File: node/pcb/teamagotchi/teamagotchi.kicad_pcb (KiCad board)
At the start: 2 copper layers, 2 parts

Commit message: first shot of the pcv
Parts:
- removed A1: Adafruit_Feather_Generic, Module:Adafruit_Feather
- removed BT1: Battery, Battery:BatteryHolder_Keystone_103_1x20mm
- added R1: R, Resistor_THT:R_Axial_DIN0204_L3.6mm_D1.6mm_P7.62mm_Horizontal, F.Cu at (173.5, 108.3)
- added R2: R, Resistor_THT:R_Axial_DIN0204_L3.6mm_D1.6mm_P7.62mm_Horizontal, F.Cu at (170.3, 108.3)
- added R3: R, Resistor_THT:R_Axial_DIN0204_L3.6mm_D1.6mm_P7.62mm_Horizontal, F.Cu at (167.2, 108.3)
- added R4: R, Resistor_THT:R_Axial_DIN0204_L3.6mm_D1.6mm_P7.62mm_Horizontal, F.Cu at (164.0, 108.3)
- added R5: R, Resistor_THT:R_Axial_DIN0204_L3.6mm_D1.6mm_P7.62mm_Horizontal, F.Cu at (160.9, 108.3)
- added REF**: MountingHole_2.2mm_M2, MountingHole:MountingHole_2.2mm_M2, F.Cu at (182.5, 49.2)
- added REF**: MountingHole_2.2mm_M2, MountingHole:MountingHole_2.2mm_M2, F.Cu at (112.5, 49.2)
- added REF**: MountingHole_2.2mm_M2, MountingHole:MountingHole_2.2mm_M2, F.Cu at (182.5, 155.6)
- added REF**: MountingHole_2.2mm_M2, MountingHole:MountingHole_2.2mm_M2, F.Cu at (112.5, 155.6)
- added SW1: SW_Push, Button_Switch_THT:SW_SPST_Omron_B3F-40xx, F.Cu at (167.4, 129.3)
- added SW2: SW_Push, Button_Switch_THT:SW_SPST_Omron_B3F-40xx, F.Cu at (130.4, 112.3)
- added SW3: SW_Push, Button_Switch_THT:SW_SPST_Omron_B3F-40xx, F.Cu at (145.9, 129.3)
- added SW4: SW_Push, Button_Switch_THT:SW_SPST_Omron_B3F-40xx, F.Cu at (114.9, 129.3)
- added SW5: SW_Push, Button_Switch_THT:SW_SPST_Omron_B3F-40xx, F.Cu at (130.4, 146.3)
- added TFT1: ~, Library:Display-2.8, F.Cu at (126.7, 92.8)
- added U1: 3406, Library:MODULE_3406, B.Cu at (156.2, 74.2)
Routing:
- net Net-(TFT1-3/5V): track 0.00 -> 185.0 mm, vias 0 -> 1
- net Net-(U1-A2/0.04): track 0.00 -> 100.9 mm
- net Net-(U1-A4/0.28): track 0.00 -> 78.4 mm
- net Net-(TFT1-GND): track 0.00 -> 75.3 mm, vias 0 -> 1
- net Net-(A1-GND): track 66.5 -> 0.00 mm
- net Net-(U1-A1/0.03): track 0.00 -> 63.3 mm
- net Net-(U1-A3/0.05): track 0.00 -> 56.6 mm
- net Net-(TFT1-D10/TFT_CS): track 0.00 -> 36.8 mm, vias 0 -> 1
- net Net-(TFT1-D9/TFT_DC): track 0.00 -> 36.4 mm
- net Net-(TFT1-D8/Touch_CS): track 0.00 -> 36.3 mm
- net Net-(A1-VBAT): track 27.8 -> 0.00 mm
- net Net-(TFT1-D13/SCLK): track 0.00 -> 25.5 mm
- net Net-(R5-Pad2): track 0.00 -> 18.5 mm
- net Net-(TFT1-D12/MISO): track 0.00 -> 15.0 mm
- net Net-(TFT1-D11/MOSI): track 0.00 -> 15.0 mm
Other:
- board outline added: 75.1 x 111.4 mm

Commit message: first 1.0 of PCB
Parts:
- removed REF** (x4): MountingHole_2.2mm_M2, MountingHole:MountingHole_2.2mm_M2
- added C1: C, Capacitor_THT:C_Disc_D3.0mm_W1.6mm_P2.50mm, B.Cu at (113.9, 79.9)
- added D1: 1N4001, Diode_THT:D_DO-41_SOD81_P10.16mm_Horizontal, B.Cu at (112.6, 67.6)
- added M1: Motor_DC, Connector_Molex:Molex_MicroClasp_55932-0210_1x02_P2.00mm_Vertical, B.Cu at (121.4, 85.1)
- added Q1: BC547, Package_TO_SOT_THT:TO-92_Inline, B.Cu at (125.6, 72.6)
- added R6: R, Resistor_THT:R_Axial_DIN0204_L3.6mm_D1.6mm_P7.62mm_Horizontal, B.Cu at (128.4, 60.6)
- moved TFT1 65.7 mm to (177.9, 51.6)
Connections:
- R5 pad 2: Net-(R5-Pad2) -> Net-(U1-A5/0.29)
- SW2 pad 1: Net-(R5-Pad2) -> Net-(U1-A5/0.29)
- U1 pad 10: unconnected-(U1-A5/0.29-Pad10) -> Net-(U1-A5/0.29)
- U1 pad 22: Net-(TFT1-D9/TFT_DC) -> Net-(TFT1-D10/TFT_CS)
- U1 pad 23: Net-(TFT1-D10/TFT_CS) -> Net-(TFT1-D9/TFT_DC)
- U1 pad 25: unconnected-(U1-P0.16-Pad25) -> Net-(U1-P0.16)
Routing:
- net Net-(U1-P0.16): track 0.00 -> 53.6 mm
- net Net-(U1-A5/0.29): track 0.00 -> 48.5 mm
- net Net-(D1-K): track 185.0 -> 214.8 mm
- net Net-(D1-A): track 0.00 -> 29.5 mm
- net Net-(TFT1-D10/TFT_CS): track 36.8 -> 12.4 mm, vias 1 -> 0
- net Net-(TFT1-D9/TFT_DC): track 36.4 -> 12.4 mm
- net Net-(TFT1-D8/Touch_CS): track 36.3 -> 12.4 mm
- net Net-(Q1-E): track 75.3 -> 96.0 mm
- net Net-(TFT1-D12/MISO): track 15.0 -> 33.9 mm
- net Net-(TFT1-D11/MOSI): track 15.0 -> 33.8 mm
- net Net-(R5-Pad2): track 18.5 -> 0.00 mm
- net Net-(TFT1-D13/SCLK): track 25.5 -> 37.0 mm, vias 0 -> 1
- net Net-(U1-A1/0.03): track 63.3 -> 71.9 mm, vias 0 -> 1
- net Net-(Q1-B): track 0.00 -> 5.00 mm
- net Net-(U1-A2/0.04): track 100.9 -> 104.5 mm
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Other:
- board size 75.1 x 111.4 mm -> 75 x 112 mm
- board text added: "R4"

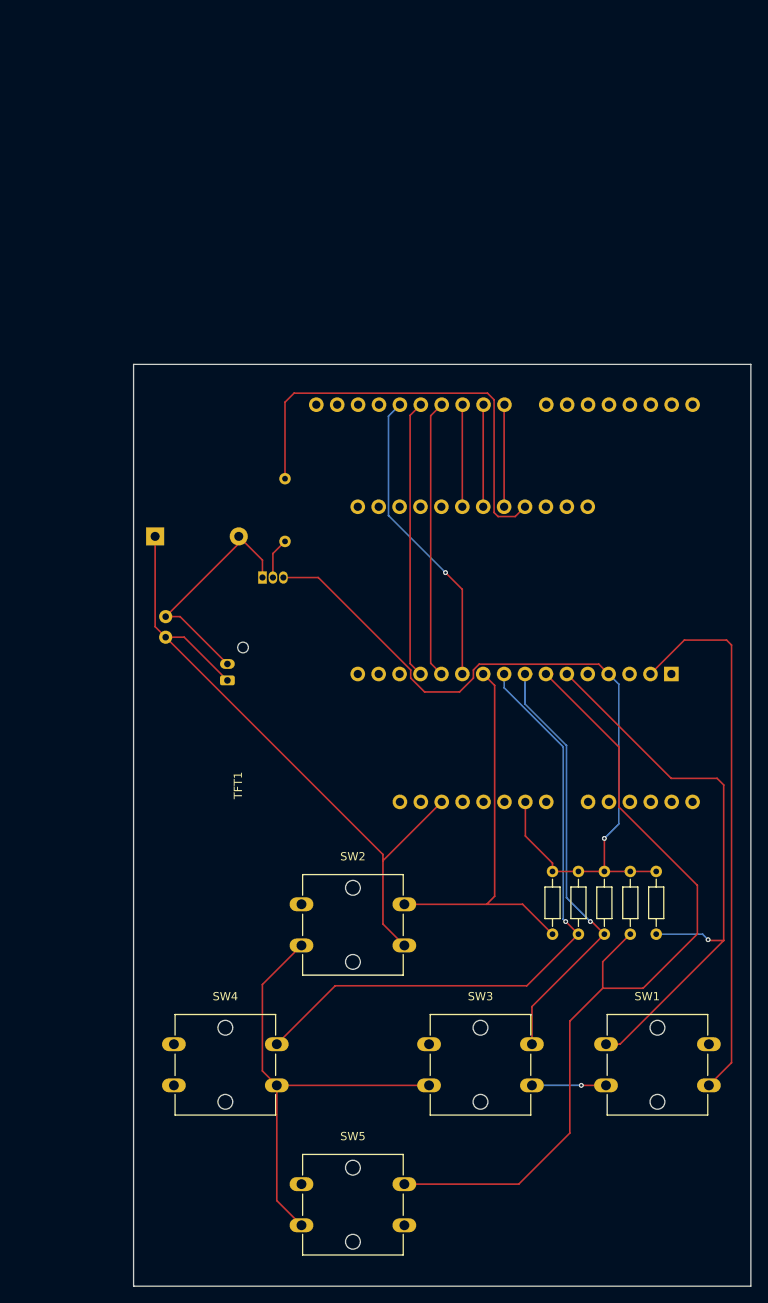
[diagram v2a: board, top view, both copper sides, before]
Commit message: added 3D export
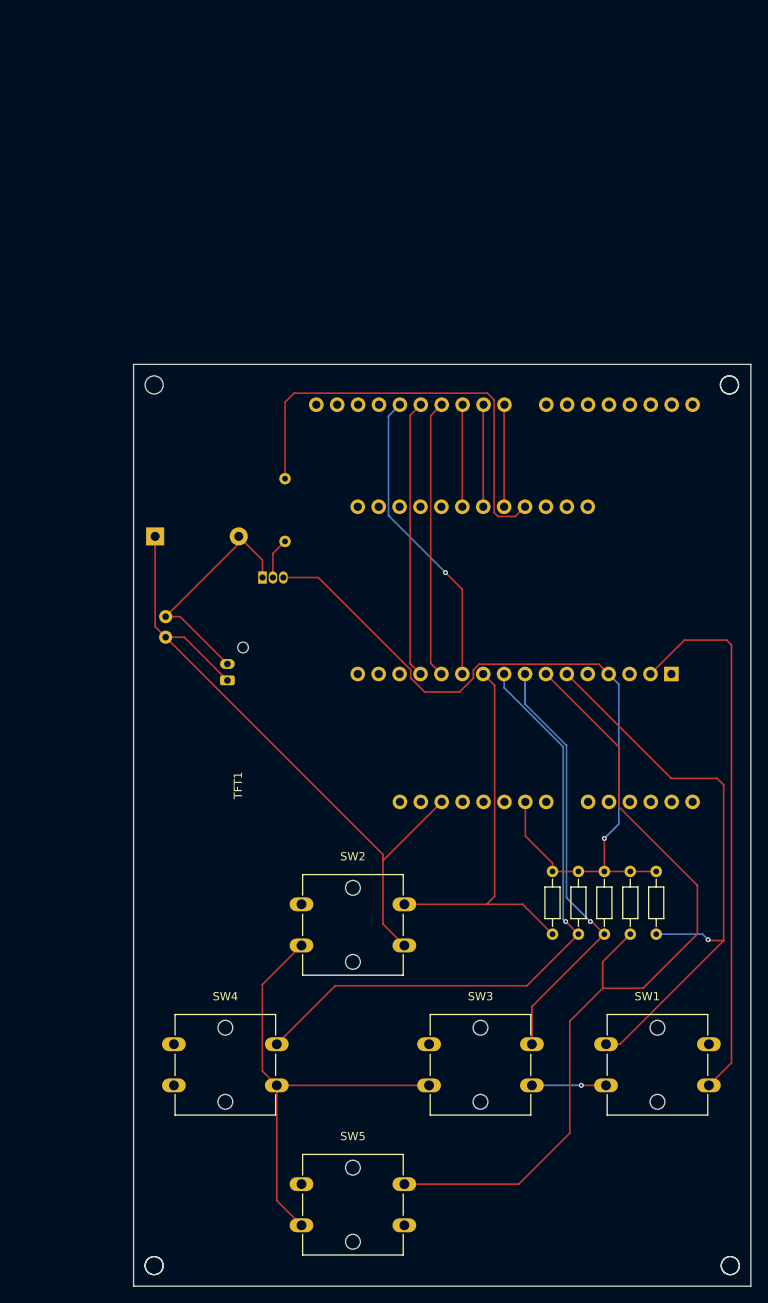
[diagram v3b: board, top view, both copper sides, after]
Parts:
- added ?: , , F.Cu at (182.4, 49.2)
- added ?: , , F.Cu at (112.5, 156.2)
- added ?: , , F.Cu at (182.5, 156.2)
- added REF**: 2.2mm_M2, MountingHole:MountingHole_2.2mm_M2, F.Cu at (112.5, 156.2)
- added REF**: 2.2mm_M2, MountingHole:MountingHole_2.2mm_M2, F.Cu at (182.5, 156.2)
- added REF**: 2.2mm_M2, MountingHole:MountingHole_2.2mm_M2, F.Cu at (112.5, 49.2)
- added REF**: 2.2mm_M2, MountingHole:MountingHole_2.2mm_M2, F.Cu at (182.4, 49.2)

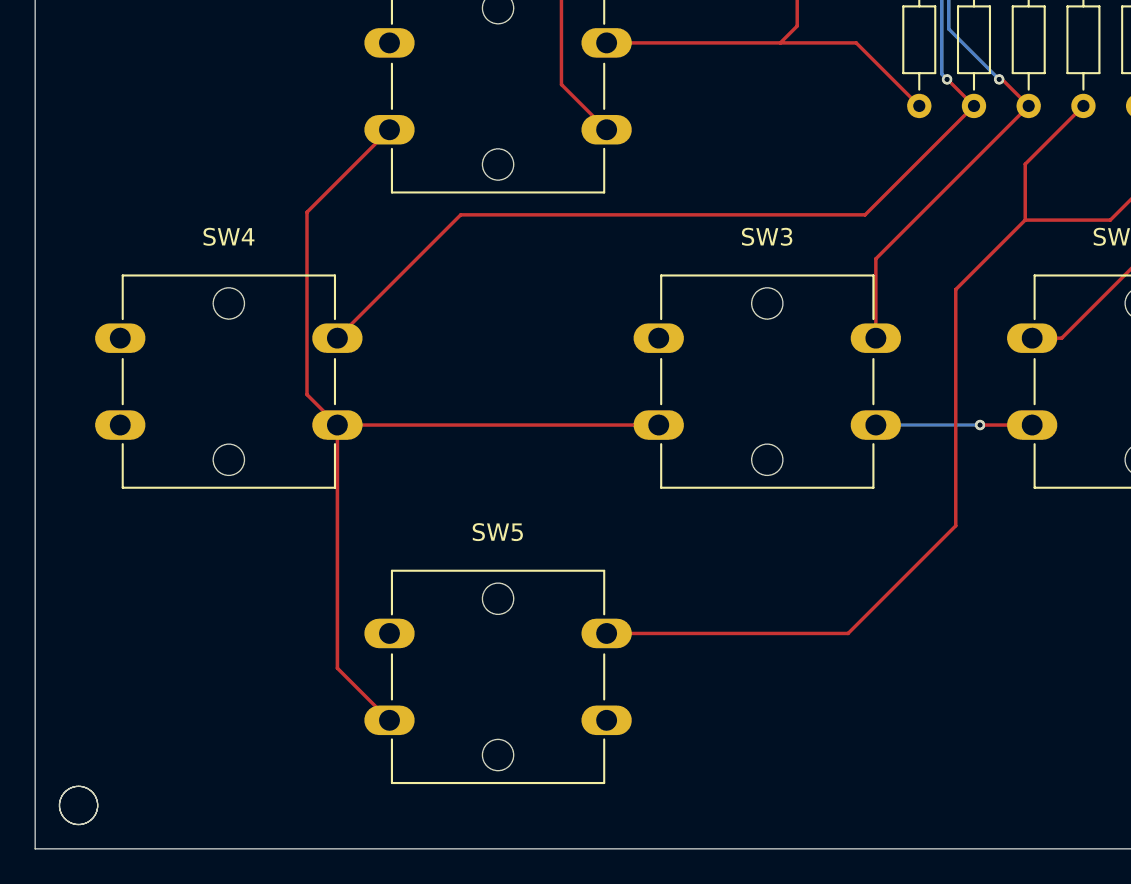
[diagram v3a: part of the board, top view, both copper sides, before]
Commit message: changed the button placement a little bit
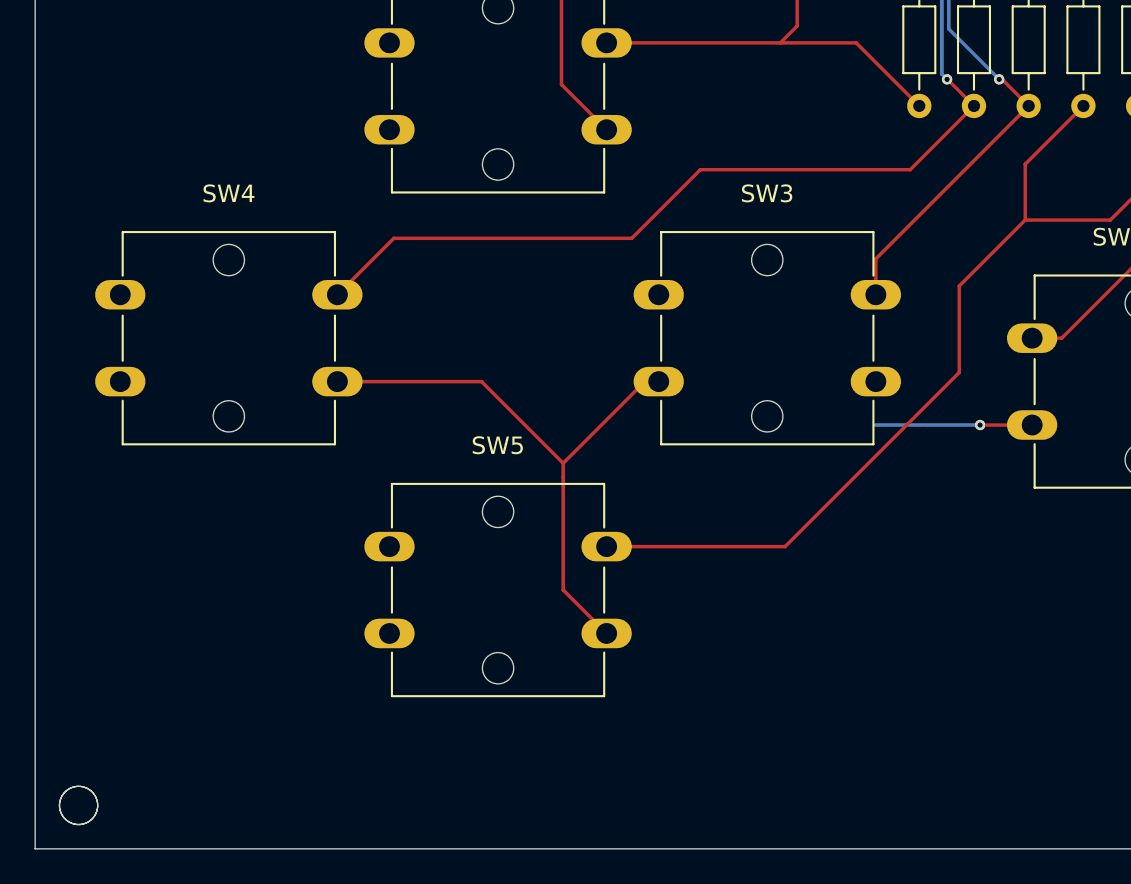
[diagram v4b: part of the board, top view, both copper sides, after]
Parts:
- moved SW5 5.00 mm to (130.4, 141.3)
- moved SW3 2.50 mm to (145.9, 126.8)
- moved SW4 2.50 mm to (114.9, 126.8)
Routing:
- net Net-(D1-K): track 214.8 -> 191.3 mm
- net Net-(U1-A2/0.04): track 104.5 -> 97.1 mm
- net Net-(U1-A3/0.05): track 53.6 -> 51.1 mm
- net Net-(U1-A4/0.28): track 77.6 -> 76.5 mm
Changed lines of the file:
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@@
 	(footprint "Button_Switch_THT:SW_SPST_Omron_B3F-40xx"
 		(layer "F.Cu")
-		(at 130.36 146.306)
+		(at 130.36 141.306)
 		(descr "SW_THT_Tactile_Omron_B3F-40xx, 12x12 mm, Through hole switch from the B3F Family manufactured by Omron,  https://www.omron.com/ecb/products/pdf/en-b3f.pdf")
 		(tags "tactile switch THT button push B3F-4000 B3F-4050 B3F-4005 B3F-4055  ")
@@
 	(footprint "Button_Switch_THT:SW_SPST_Omron_B3F-40xx"
 		(layer "F.Cu")
-		(at 145.86 129.306)
+		(at 145.86 126.806)
 		(descr "SW_THT_Tactile_Omron_B3F-40xx, 12x12 mm, Through hole switch from the B3F Family manufactured by Omron,  https://www.omron.com/ecb/products/pdf/en-b3f.pdf")
 		(tags "tactile switch THT button push B3F-4000 B3F-4050 B3F-4005 B3F-4055  ")
@@
 	(footprint "Button_Switch_THT:SW_SPST_Omron_B3F-40xx"
 		(layer "F.Cu")
-		(at 114.86 129.306)
+		(at 114.86 126.806)
 		(descr "SW_THT_Tactile_Omron_B3F-40xx, 12x12 mm, Through hole switch from the B3F Family manufactured by Omron,  https://www.omron.com/ecb/products/pdf/en-b3f.pdf")
 		(tags "tactile switch THT button push B3F-4000 B3F-4050 B3F-4005 B3F-4055  ")
@@
 	)
 	(segment
-		(start 158.36 129.306)
-		(end 158.36 124.736)
+		(start 158.36 124.736)
+		(end 167.16 115.936)
 		(width 0.2)
 		(layer "F.Cu")
@@
 	)
 	(segment
-		(start 165.63 114.406)
-		(end 167.16 115.936)
+		(start 158.36 126.806)
+		(end 158.36 124.736)
 		(width 0.2)
 		(layer "F.Cu")
@@
 	)
 	(segment
-		(start 158.36 124.736)
+		(start 165.63 114.406)
 		(end 167.16 115.936)
 		(width 0.2)
@@
 	)
 	(segment
-		(start 166.96 122.506)
-		(end 166.96 119.286)
+		(start 142.86 141.306)
+		(end 153.133654 141.306)
 		(width 0.2)
 		(layer "F.Cu")
@@
 	)
 	(segment
-		(start 160.06 84.326)
-		(end 160.9185 84.326)
+		(start 163.16 131.279654)
+		(end 163.16 126.306)
 		(width 0.2)
 		(layer "F.Cu")
@@
 	)
 	(segment
-		(start 168.929 100.475)
-		(end 168.929 93.195)
+		(start 166.96 122.506)
+		(end 166.96 119.286)
 		(width 0.2)
 		(layer "F.Cu")
@@
 	)
 	(segment
-		(start 171.86 122.506)
-		(end 178.46 115.906)
+		(start 160.06 84.326)
+		(end 160.9185 84.326)
 		(width 0.2)
 		(layer "F.Cu")
@@
 	)
 	(segment
-		(start 162.96 140.106)
-		(end 162.96 126.506)
+		(start 168.929 100.475)
+		(end 168.929 93.195)
 		(width 0.2)
 		(layer "F.Cu")
@@
 	)
 	(segment
-		(start 142.86 146.306)
-		(end 156.76 146.306)
+		(start 171.86 122.506)
+		(end 178.46 115.906)
 		(width 0.2)
 		(layer "F.Cu")
@@
 	)
 	(segment
-		(start 162.96 126.506)
-		(end 166.96 122.506)
-		(width 0.2)
-		(layer "F.Cu")
-		(net 23)
-	)
-	(segment
 		(start 178.46 115.906)
 		(end 178.46 110.006)
@@
 	)
 	(segment
-		(start 156.76 146.306)
-		(end 162.96 140.106)
+		(start 163.16 126.306)
+		(end 166.96 122.506)
 		(width 0.2)
 		(layer "F.Cu")
@@
 	)
 	(segment
-		(start 142.86 146.306)
-		(end 143.11 146.056)
+		(start 153.133654 141.306)
+		(end 163.16 131.279654)
 		(width 0.2)
 		(layer "F.Cu")
@@
 	)
 	(segment
-		(start 157.74 122.206)
+		(start 160.34 119.606)
 		(end 164.01 115.936)
 		(width 0.2)
@@
 	)
 	(segment
-		(start 134.46 122.206)
-		(end 157.74 122.206)
+		(start 144.31 123.556)
+		(end 148.26 119.606)
 		(width 0.2)
 		(layer "F.Cu")
@@
 	)
 	(segment
-		(start 164.01 115.936)
-		(end 162.48 114.406)
+		(start 130.61 123.556)
+		(end 144.31 123.556)
+		(width 0.2)
+		(layer "F.Cu")
+		(net 24)
+	)
+	(segment
+		(start 127.36 126.806)
+		(end 130.61 123.556)
+		(width 0.2)
+		(layer "F.Cu")
+		(net 24)
+	)
+	(segment
+		(start 148.26 119.606)
+		(end 160.34 119.606)
 		(width 0.2)
 		(layer "F.Cu")
@@
 	)
 	(segment
-		(start 127.36 129.306)
-		(end 134.46 122.206)
+		(start 164.01 115.936)
+		(end 162.48 114.406)
 		(width 0.2)
 		(layer "F.Cu")
@@
 	)
 	(segment
-		(start 125.61 122.056)
-		(end 125.61 132.556)
+		(start 145.06 131.806)
+		(end 145.86 131.806)
+		(width 0.2)
+		(layer "F.Cu")
+		(net 27)
+	)
+	(segment
+		(start 127.36 131.806)
+		(end 135.66 131.806)
+		(width 0.2)
+		(layer "F.Cu")
+		(net 27)
+	)
+	(segment
+		(start 140.36 136.506)
+		(end 140.36 137.306)
 		(width 0.2)
 		(layer "F.Cu")
@@
 	)
 	(segment
-		(start 125.61 132.556)
-		(end 127.36 134.306)
+		(start 135.66 131.806)
+		(end 140.36 136.506)
 		(width 0.2)
 		(layer "F.Cu")
@@
 	)
 	(segment
+		(start 140.36 136.506)
+		(end 145.06 131.806)
+		(width 0.2)
+		(layer "F.Cu")
+		(net 27)
+	)
+	(segment
 		(start 113.86 79.856)
 		(end 112.58 78.576)
@@
 	)
 	(segment
-		(start 127.36 134.306)
-		(end 127.96 134.306)
+		(start 140.36 143.806)
+		(end 140.36 137.306)
 		(width 0.2)
 		(layer "F.Cu")
@@
 	)
 	(segment
-		(start 130.36 117.306)
-		(end 125.61 122.056)
-		(width 0.2)
-		(layer "F.Cu")
-		(net 27)
-	)
-	(segment
 		(start 116.11 79.856)
 		(end 121.36 85.106)
@@
 	)
 	(segment
-		(start 127.36 148.306)
-		(end 127.36 134.306)
+		(start 142.86 146.306)
+		(end 140.36 143.806)
 		(width 0.2)
 		(layer "F.Cu")
@@
 	)
 	(segment
-		(start 145.86 134.306)
-		(end 127.36 134.306)
-		(width 0.2)
-		(layer "F.Cu")
-		(net 27)
-	)
-	(segment
 		(start 182.61 131.556)
 		(end 179.86 134.306)
@@
 	)
 	(segment
-		(start 130.36 151.306)
-		(end 127.36 148.306)
+		(start 142.86 146.306)
+		(end 143.11 146.056)
 		(width 0.2)
 		(layer "F.Cu")

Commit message: some changes and renders
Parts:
- moved Q1 4.59 mm to (122.1, 75.5)
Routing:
- net Net-(Q1-B): track 5.00 -> 9.40 mm
- net Net-(D1-A): track 29.5 -> 31.5 mm
- net Net-(Q1-E): track 96.0 -> 97.8 mm
- net Net-(D1-K): track 191.3 -> 192.3 mm
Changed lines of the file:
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@@
 			(outputformat 1)
 			(mirror no)
-			(drillshape 1)
+			(drillshape 0)
 			(scaleselection 1)
-			(outputdirectory "")
+			(outputdirectory "gbr/")
 		)
 	)
@@
 			)
 		)
-		(sheetname "Stammblatt")
-		(sheetfile "teamagotchi.kicad_sch")
 		(attr through_hole)
 		(fp_rect
@@
 			(size 1.778 1.778)
 			(drill 1)
-			(layers "*.Cu" "*.Mask" "B.SilkS")
+			(layers "*.Cu" "*.Mask")
 			(remove_unused_layers no)
 		)
@@
 	(footprint "Package_TO_SOT_THT:TO-92_Inline"
 		(layer "B.Cu")
-		(at 125.62 72.606)
+		(at 122.09 75.546)
 		(descr "TO-92 leads in-line, narrow, oval pads, drill 0.75mm (see NXP sot054_po.pdf)")
 		(tags "to-92 sc-43 sc-43a sot54 PA33 transistor")
@@
 	)
 	(segment
-		(start 115.61 77.356)
-		(end 121.36 83.106)
+		(start 122.09 68.256)
+		(end 122.74 67.606)
 		(width 0.2)
 		(layer "F.Cu")
@@
 	)
 	(segment
-		(start 125.62 70.486)
-		(end 122.74 67.606)
+		(start 115.61 77.356)
+		(end 121.36 83.106)
 		(width 0.2)
 		(layer "F.Cu")
@@
 	(segment
 		(start 113.86 77.356)
-		(end 122.74 68.476)
+		(end 113.86 76.486)
 		(width 0.2)
 		(layer "F.Cu")
@@
 	)
 	(segment
-		(start 125.62 72.606)
-		(end 125.62 70.486)
+		(start 113.86 76.486)
+		(end 122.74 67.606)
 		(width 0.2)
 		(layer "F.Cu")
@@
 	)
 	(segment
-		(start 122.74 68.476)
-		(end 122.74 67.606)
+		(start 122.09 75.546)
+		(end 122.09 68.256)
 		(width 0.2)
 		(layer "F.Cu")
@@
 	(segment
 		(start 164.36 134.306)
-		(end 158.36 134.306)
+		(end 161.86 131.806)
 		(width 0.2)
 		(layer "B.Cu")
@@
 	)
 	(segment
-		(start 126.89 69.686)
-		(end 128.36 68.216)
+		(start 161.86 131.806)
+		(end 158.36 131.806)
 		(width 0.2)
-		(layer "F.Cu")
-		(net 28)
+		(layer "B.Cu")
+		(net 27)
 	)
 	(segment
-		(start 126.89 72.606)
-		(end 126.89 69.686)
+		(start 123.36 75.546)
+		(end 123.36 73.216)
 		(width 0.2)
 		(layer "F.Cu")
@@
 	)
 	(segment
-		(start 132.4035 72.606)
-		(end 143.631 83.8335)
+		(start 123.36 73.216)
+		(end 128.36 68.216)
 		(width 0.2)
 		(layer "F.Cu")
-		(net 29)
+		(net 28)
 	)
 	(segment
-		(start 145.3185 86.506)
-		(end 149.5635 86.506)
+		(start 124.63 75.546)
+		(end 135.29 86.206)
 		(width 0.2)
 		(layer "F.Cu")
@@
 	)
 	(segment
-		(start 143.631 84.8185)
-		(end 145.3185 86.506)
+		(start 166.491 83.137)
+		(end 167.68 84.326)
 		(width 0.2)
 		(layer "F.Cu")
@@
 	)
 	(segment
-		(start 160.86 108.316)
-		(end 164.01 108.316)
+		(start 149.8635 86.206)
+		(end 151.16 84.9095)
 		(width 0.2)
 		(layer "F.Cu")
@@
 	)
 	(segment
-		(start 149.5635 86.506)
-		(end 151.251 84.8185)
+		(start 151.16 84.9095)
+		(end 151.16 83.406)
 		(width 0.2)
 		(layer "F.Cu")
@@
 	)
 	(segment
-		(start 167.16 108.316)
-		(end 167.16 104.306)
+		(start 135.29 86.206)
+		(end 149.8635 86.206)
 		(width 0.2)
 		(layer "F.Cu")
@@
 	)
 	(segment
-		(start 167.16 108.316)
+		(start 160.86 108.316)
 		(end 164.01 108.316)
 		(width 0.2)
@@
 	)
 	(segment
-		(start 128.16 72.606)
-		(end 132.4035 72.606)
-		(width 0.2)
-		(layer "F.Cu")
-		(net 29)
-	)
-	(segment
-		(start 143.631 83.8335)
-		(end 143.631 84.8185)
+		(start 167.16 108.316)
+		(end 167.16 104.306)
 		(width 0.2)
 		(layer "F.Cu")
@@
 	)
 	(segment
-		(start 151.251 84.8185)
-		(end 151.251 83.8335)
+		(start 167.16 108.316)
+		(end 164.01 108.316)
 		(width 0.2)
 		(layer "F.Cu")
@@
 	)
 	(segment
-		(start 151.9475 83.137)
+		(start 151.429 83.137)
 		(end 166.491 83.137)
 		(width 0.2)
@@
 	)
 	(segment
-		(start 166.491 83.137)
-		(end 167.68 84.326)
+		(start 151.16 83.406)
+		(end 151.429 83.137)
 		(width 0.2)
 		(layer "F.Cu")
@@
 		(width 0.2)
 		(layer "F.Cu")
-		(net 29)
-	)
-	(segment
-		(start 151.251 83.8335)
-		(end 151.9475 83.137)
-		(width 0.2)
-		(layer "F.Cu")

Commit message: added a connection
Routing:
- net Net-(D1-K): track 192.3 -> 208.1 mm
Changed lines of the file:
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@@
+	)
+	(segment
+		(start 142.86 128.806)
+		(end 145.86 131.806)
+		(width 0.2)
+		(layer "B.Cu")
+		(net 27)
 	)
 	(segment
@@
 		(width 0.2)
 		(layer "B.Cu")
+		(net 27)
+	)
+	(segment
+		(start 142.86 117.306)
+		(end 142.86 128.806)
+		(width 0.2)
+		(layer "B.Cu")
